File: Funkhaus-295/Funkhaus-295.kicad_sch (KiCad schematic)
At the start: 69 parts, among them SW1 SW_DPDT_x2, SW2 SW_Rotary2x6, U1 TL072, U2 TL072, U3 TL072, U4 TL072, U5 TL072

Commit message: updated schematic
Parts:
- added R2: (no value), Resistor_THT:R_Axial_DIN0207_L6.3mm_D2.5mm_P10.16mm_Horizontal, symbol Device:R
- C17: value 15n -> (none)
- C7: value 150n -> (none)
- R23: value 2k5 -> (none)
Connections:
- net at C21.1, C4.1, RV1.3: now also R23.1, RV1.2; no longer R23.2
- net at SW1.2 (B): now also RV1.1; no longer R23.1
- new net: R2.1, R23.2
- new net: R2.2, SW1.5 (B)
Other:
- title: Funkaus EQ -> Funkhaus EQ
- moved on the sheet: R23, RV1, SW1A, SW1B

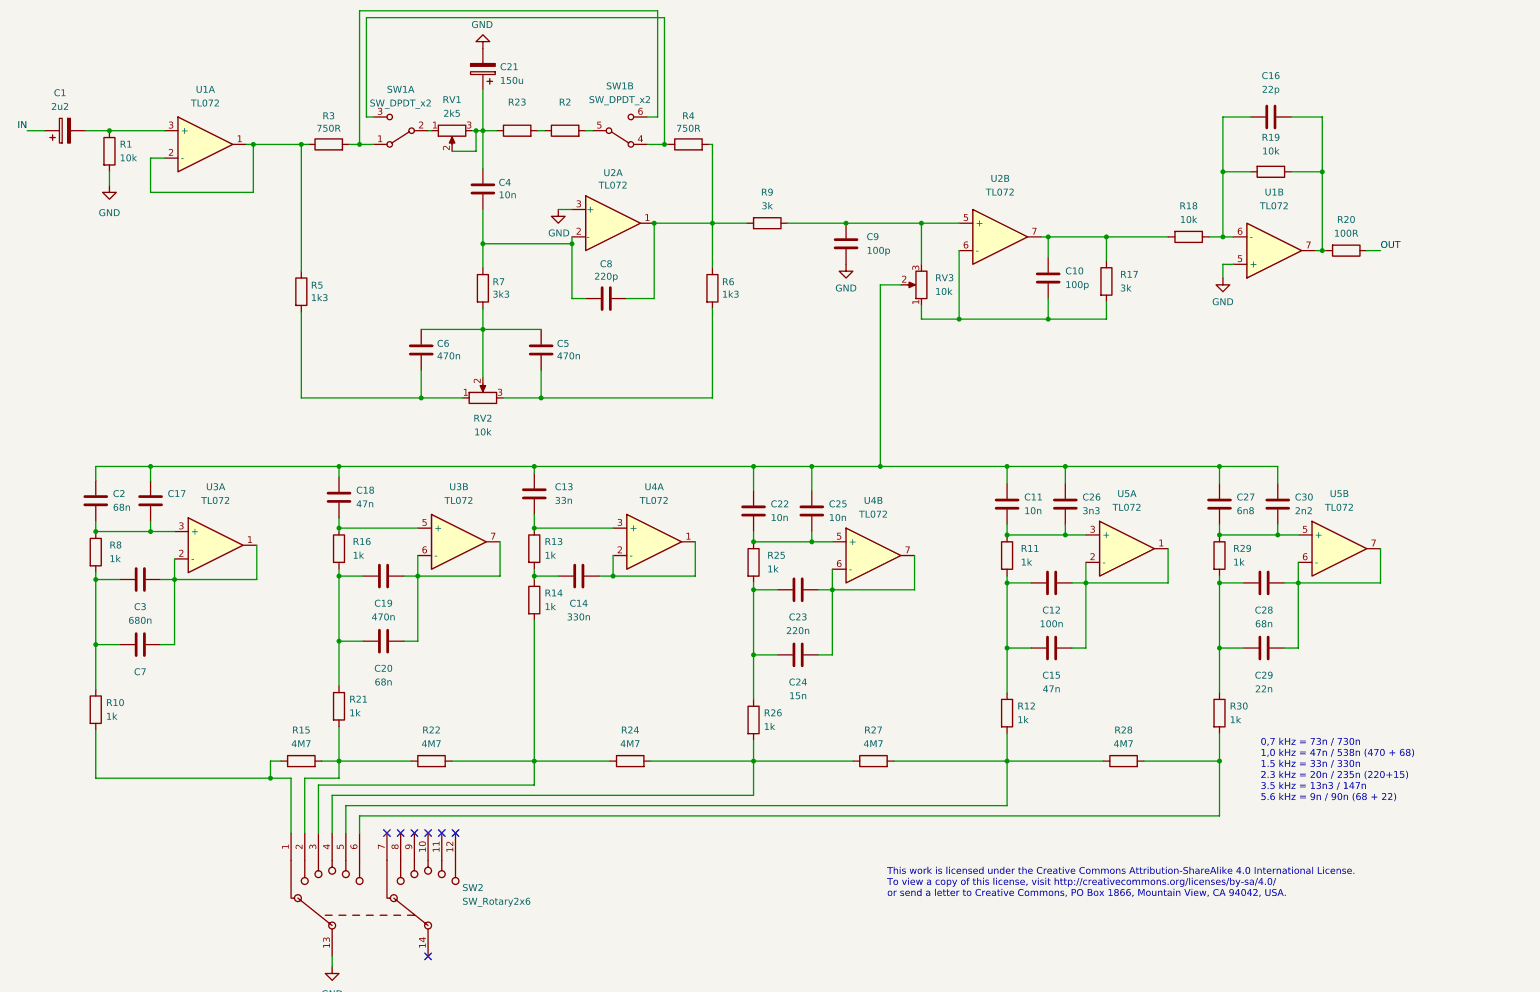
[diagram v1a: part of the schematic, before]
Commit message: added Q-Mod circuit, changed project name
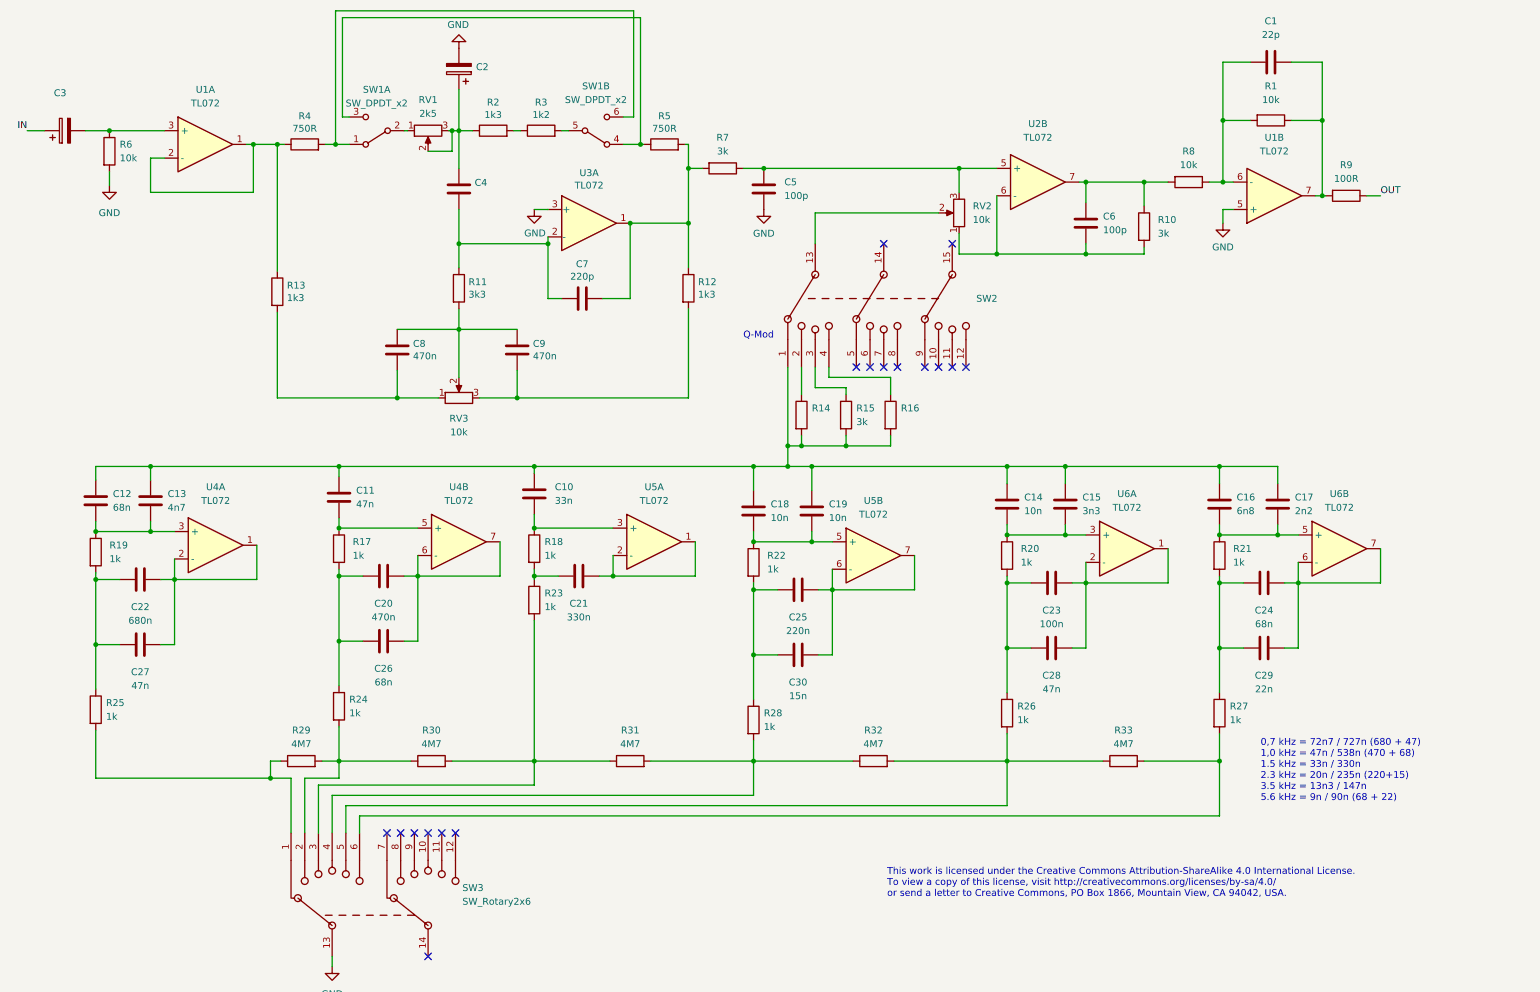
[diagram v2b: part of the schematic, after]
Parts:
- added R14, R16: (no value), symbol Device:R
- added R15: 3k, symbol Device:R
- added SW2: (no value), symbol Switch:SW_Rotary3x4
- C13: renamed from C17; value (none) -> 4n7
- C2: renamed from C21; value 150u -> (none)
- C27: renamed from C7; value (none) -> 47n
- C3: renamed from C1; value 2u2 -> (none)
- C4: value 10n -> (none); footprint Capacitor_THT:C_Rect_L10.0mm_W3.0mm_P7.50mm_MKS4 -> (none)
- R2: renamed from R23; value (none) -> 1k3
- R3: renamed from R2; value (none) -> 1k2
- renumbered C16 to C1, C13 to C10, C18 to C11, C2 to C12, C11 to C14, C26 to C15, C27 to C16, C30 to C17, C22 to C18, C25 to C19, C19 to C20, C14 to C21, C3 to C22, C12 to C23, C28 to C24, C23 to C25, C20 to C26, C15 to C28, C24 to C30, C9 to C5, C10 to C6, C8 to C7, C6 to C8, C5 to C9, R19 to R1, R17 to R10, R7 to R11, R6 to R12, R5 to R13, R16 to R17, R13 to R18, R8 to R19, R11 to R20, R29 to R21, R25 to R22, R14 to R23, R21 to R24, R10 to R25, R12 to R26, R30 to R27, R26 to R28, R15 to R29, R22 to R30, R24 to R31, R27 to R32, R28 to R33, R3 to R4, R4 to R5, R1 to R6, R9 to R7, R18 to R8, R20 to R9, RV3 to RV2, RV2 to RV3, SW2 to SW3, U2 to U3, U3 to U4, U4 to U5, U5 to U6
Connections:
- net at C10.1, C11.1, C12.1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: now also R14.2, R15.2, R16.2, SW2.1; no longer RV2.2
- new net: R15.1, SW2.3
- new net: R14.1, SW2.2
- new net: R16.1, SW2.4
- new net: RV2.2, SW2.13
- no-connect marks 7 -> 17
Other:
- note added: "0,7 kHz = 72n7 / 727n (680 + 47) 1,0 kHz = 47n / 538n (470 + 68) 1.5 kHz = 33n / 330n 2.3 kHz = 20n / 235n (220+15) 3.5 kHz = 13n3 / 147n 5.6 kHz = 9n / 90n (68 + 22)"
- note added: "Q-Mod"
- note removed: "0,7 kHz = 73n / 730n 1,0 kHz = 47n / 538n (470 + 68) 1.5 kHz = 33n / 330n 2.3 kHz = 20n / 235n (220+15) 3.5 kHz = 13n3 / 147n 5.6 kHz = 9n / 90n (68 + 22)"
- title: Funkhaus EQ -> SIAM 295b
- moved on the sheet: C1, C2, C4, C5, C6, C7, C8, C9, R1, R10, R11, R12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

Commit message: updated schematic
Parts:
- C2: value (none) -> 150u
- C3: value (none) -> 4u7
- C4: value (none) -> 10n; footprint (none) -> Capacitor_THT:C_Rect_L10.0mm_W3.0mm_P7.50mm_MKS4
- C7: value 220p -> (none); footprint Capacitor_THT:C_Disc_D5.0mm_W2.5mm_P5.00mm -> (none)
- R14: value (none) -> 1k
- R16: value (none) -> ~
- SW2: value (none) -> SW_Rotary3x4
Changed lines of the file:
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@@
   (title_block
     (title "SIAM 295b")
-    (date "2022-03-29")
-    (rev "03")
+    (date "2022-04-02")
+    (rev "04")
     (company "Robert-André Vettel")
   )
@@
     (in_bom yes) (on_board yes)
     (property "Reference" "C7" (id 0) (at 122.555 60.2742 90))
-    (property "Value" "220p" (id 1) (at 122.555 62.5856 90))
-    (property "Footprint" "Capacitor_THT:C_Disc_D5.0mm_W2.5mm_P5.00mm" (id 2) (at 126.365 65.7098 0)
+    (property "Value" "" (id 1) (at 122.555 62.5856 90))
+    (property "Footprint" "" (id 2) (at 126.365 65.7098 0)
       (effects (font (size 1.27 1.27)) hide)
     )
@@
       (effects (font (size 1.27 1.27)) (justify left))
     )
-    (property "Value" "" (id 1) (at 102.616 47.498 0)
-      (effects (font (size 1.27 1.27)) (justify left))
-    )
-    (property "Footprint" "" (id 2) (at 100.6602 50.165 0)
+    (property "Value" "10n" (id 1) (at 102.616 47.498 0)
+      (effects (font (size 1.27 1.27)) (justify left))
+    )
+    (property "Footprint" "Capacitor_THT:C_Rect_L10.0mm_W3.0mm_P7.50mm_MKS4" (id 2) (at 100.6602 50.165 0)
       (effects (font (size 1.27 1.27)) hide)
     )
@@
       (effects (font (size 1.27 1.27)) (justify left))
     )
-    (property "Value" "" (id 1) (at 165.1 89.5349 0)
+    (property "Value" "1k" (id 1) (at 165.1 89.5349 0)
       (effects (font (size 1.27 1.27)) (justify left))
     )
@@
       (effects (font (size 1.27 1.27)) (justify left))
     )
-    (property "Value" "" (id 1) (at 181.61 89.5349 0)
+    (property "Value" "~" (id 1) (at 181.61 89.5349 0)
       (effects (font (size 1.27 1.27)) (justify left))
     )
@@
     (in_bom yes) (on_board yes) (fields_autoplaced)
     (property "Reference" "C3" (id 0) (at 25.781 28.575 90))
-    (property "Value" "" (id 1) (at 25.781 31.115 90))
+    (property "Value" "4u7" (id 1) (at 25.781 31.115 90))
     (property "Footprint" "" (id 2) (at 30.48 34.5948 0)
       (effects (font (size 1.27 1.27)) hide)
@@
       (effects (font (size 1.27 1.27)) (justify right))
     )
-    (property "Value" "" (id 1) (at 102.87 26.2889 0)
+    (property "Value" "150u" (id 1) (at 102.87 26.2889 0)
       (effects (font (size 1.27 1.27)) (justify right))
     )
@@
       (effects (font (size 1.27 1.27)) (justify right))
     )
-    (property "Value" "" (id 1) (at 195.58 69.2149 90)
+    (property "Value" "SW_Rotary3x4" (id 1) (at 195.58 69.2149 90)
       (effects (font (size 1.27 1.27)) (justify right))
     )
@@
     )
     (path "/00000000-0000-0000-0000-00005bc8d424"
-      (reference "C7") (unit 1) (value "220p") (footprint "Capacitor_THT:C_Disc_D5.0mm_W2.5mm_P5.00mm")
+      (reference "C7") (unit 1) (value "330p") (footprint "Capacitor_THT:C_Disc_D5.0mm_W2.5mm_P5.00mm")
     )
     (path "/00000000-0000-0000-0000-00005bcf4f4d"
@@
       (reference "R15") (unit 1) (value "3k") (footprint "")
     )
-    (path "/52428705-e432-48e4-9039-961cc5bc7d28"
-      (reference "R16") (unit 1) (value "10k") (footprint "")
+    (path "/52428705-e432-48e4-9039-961cc5bc7d29"
+      (reference "R16") (unit 1) (value "~") (footprint "")
     )
     (path "/95e52724-0270-4ea6-b702-bac6694d6a0d"

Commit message: updated schematic
rev 05
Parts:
- removed U1, U2, U4, U5, U6: TL072, symbol Device:Opamp_Dual
- removed U3: TL072, symbol Amplifier_Operational:LM4562
- added C31, C34: 10u, symbol Device:C_Polarized_Small
- added C32, C33, C35, C36, C37, C38: 100n, Capacitor_THT:C_Rect_L10.0mm_W3.0mm_P7.50mm_MKS4, symbol Device:C
- added C39, C41: 2n2, symbol Device:C
- added C40: 220p, symbol Device:C
- added R34: 3k, symbol Device:R
- added R35: 3k3, symbol Device:R
- added R36: 27k, symbol Device:R
- added U1, U2, U3: TL074, symbol Amplifier_Operational:TL074
- C3: value 4u7 -> 2u2
- C7: value (none) -> 220p; footprint (none) -> Capacitor_THT:C_Disc_D5.0mm_W2.5mm_P5.00mm
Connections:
- net GND: now also R23.2, R24.2, R25.2, R26.2, R27.2, R28.2, C31.2, C32.2, C33.2, C34.1, C35.2, C36.2, C37.2, C38.2, C39.2, C40.2, U1.12 (+), U3.5 (+); no longer SW3.13
- net at C7.2, R12.1, R5.2: now also R34.2; no longer R7.2
- net at R13.1, R4.1: now also U1.1, U1.2 (-)
- net at C5.1, R7.1, RV2.3: now also U3.3 (+)
- net at C6.2, R10.2, RV2.1: now also U3.2 (-)
- net at C6.1, R10.1, R8.2: now also U3.1
- net at C24.2, C29.2: now also U3.8, U3.9 (-)
- net at C25.2, C30.2: now also U2.1, U2.2 (-)
- net at C16.2, C17.2, R21.1: now also U3.10 (+)
- net at C22.2, C27.2: now also U1.6 (-), U1.7
- net at C3.2, R6.1: now also U1.3 (+)
- net at R29.1, SW3.1: now also C12.1, C13.1; no longer R25.2
- net at C14.2, C15.2, R20.1: now also U2.5 (+)
- net at C23.2, C28.2: now also U2.6 (-), U2.7
- net at R30.2, R31.1, SW3.3: now also C10.1; no longer R23.2
- net at R31.2, R32.1, SW3.4: now also C18.1, C19.1; no longer R28.2
- net at R32.2, R33.1, SW3.5: now also C14.1, C15.1; no longer R26.2
- net at C12.2, C13.2, R19.1: now also U1.5 (+)
- net at C20.2, C26.2: now also U2.8, U2.9 (-)
- net at C11.2, R17.1: now also U2.10 (+)
- net at C21.2: now also U3.13 (-), U3.14
- net at C18.2, C19.2, R22.1: now also U2.3 (+)
- net at R29.2, R30.1, SW3.2: now also C11.1; no longer R24.2
- net at R33.2, SW3.6: now also C16.1, C17.1; no longer R27.2
- net at C10.2, R18.1: now also U3.12 (+)
- net at C1.1, R1.2, R8.1: now also U3.6 (-)
- net at C1.2, R1.1, R9.2: now also U3.7
- new net: R14.2, R15.2, R16.2, SW2.1, SW3.13
- new net: C39.1, R34.1, U1.10 (+)
- new net: C41.2, R7.2, U2.13 (-), U2.14
- new net: C40.1, R36.1, U2.12 (+)
- new net: C41.1, R35.1, R36.2
- new net: R35.2, U1.8, U1.9 (-)
- new net: U1.13 (-), U1.14
- new net +12V: C31.1, C32.1, C35.1, C37.1, U1.4 (V+), U2.4 (V+), U3.4 (V+)
- new net -12V: C33.1, C34.2, C36.1, C38.1, U1.11 (V-), U2.11 (V-), U3.11 (V-)
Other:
- moved on the sheet: C1, C10, C11, C12, C13, C14, C15, C16, C17, C18, C19, C2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

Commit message: Rev 05a
- added a missing OpAmp
- added a cat
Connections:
- net GND: now also U1.13 (-), U1.5 (+); no longer U1.12 (+), U3.5 (+)
- net at C4.2, C7.1, R11.1: now also U1.6 (-)
- net at C7.2, R12.1, R34.2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: now also U1.7
- net at C24.2, C29.2: now also U3.13 (-), U3.14; no longer U3.8, U3.9 (-)
- net at C25.2, C30.2: now also U3.5 (+), U3.7; no longer U2.1, U2.2 (-)
- net at C5.1, R7.1, RV2.3: now also U1.10 (+); no longer U3.3 (+)
- net at C16.2, C17.2, R21.1: now also U3.12 (+); no longer U3.10 (+)
- net at C39.1, R34.1: now also U2.3 (+); no longer U1.10 (+)
- net at C41.2, R7.2: now also U2.6 (-), U2.7; no longer U2.13 (-), U2.14
- net at C11.2, R17.1: now also U2.12 (+); no longer U2.10 (+)
- net at U2.8, U2.9 (-): now also C22.2, C27.2; no longer C20.2, C26.2
- net at C40.1, R36.1: now also U2.5 (+); no longer U2.12 (+)
- net at C14.2, C15.2, R20.1: now also U3.10 (+); no longer U2.5 (+)
- net at C23.2, C28.2: now also U3.8, U3.9 (-); no longer U2.6 (-), U2.7
- net at C12.2, C13.2, R19.1: now also U2.10 (+); no longer U1.5 (+)
- net at C18.2, C19.2, R22.1: now also U3.6 (-); no longer U2.3 (+)
- net at C10.2, R18.1: now also U3.3 (+); no longer U3.12 (+)
- net at U1.14: now also C1.2, R1.1, R9.2; no longer U1.13 (-)
- net at C1.1, R1.2, R8.1: now also U1.12 (+); no longer U3.6 (-)
- net at C6.1, R10.1, R8.2: now also U1.8; no longer U3.1
- net at C6.2, R10.2, RV2.1: now also U1.9 (-); no longer U3.2 (-)
- new net: C20.2, C26.2, U2.13 (-), U2.14
- new net: C21.2, U3.1, U3.2 (-)
- new net: R35.2, U2.1, U2.2 (-)
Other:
- moved on the sheet: C2, C31, C32, C33, C34, C35, C36, C37, C38, C4, C7, R11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
